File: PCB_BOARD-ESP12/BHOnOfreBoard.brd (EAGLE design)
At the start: 53 x 55 mm, 23 parts, among them J1 4p, J6 8p, J7 8p, K1 OMRON-G3MB-202P-SSR2, K2 OMRON-G3MB-202P-SSR2, Q1 S8050, Q2 S8050, U1 LM1117, U2 esp12

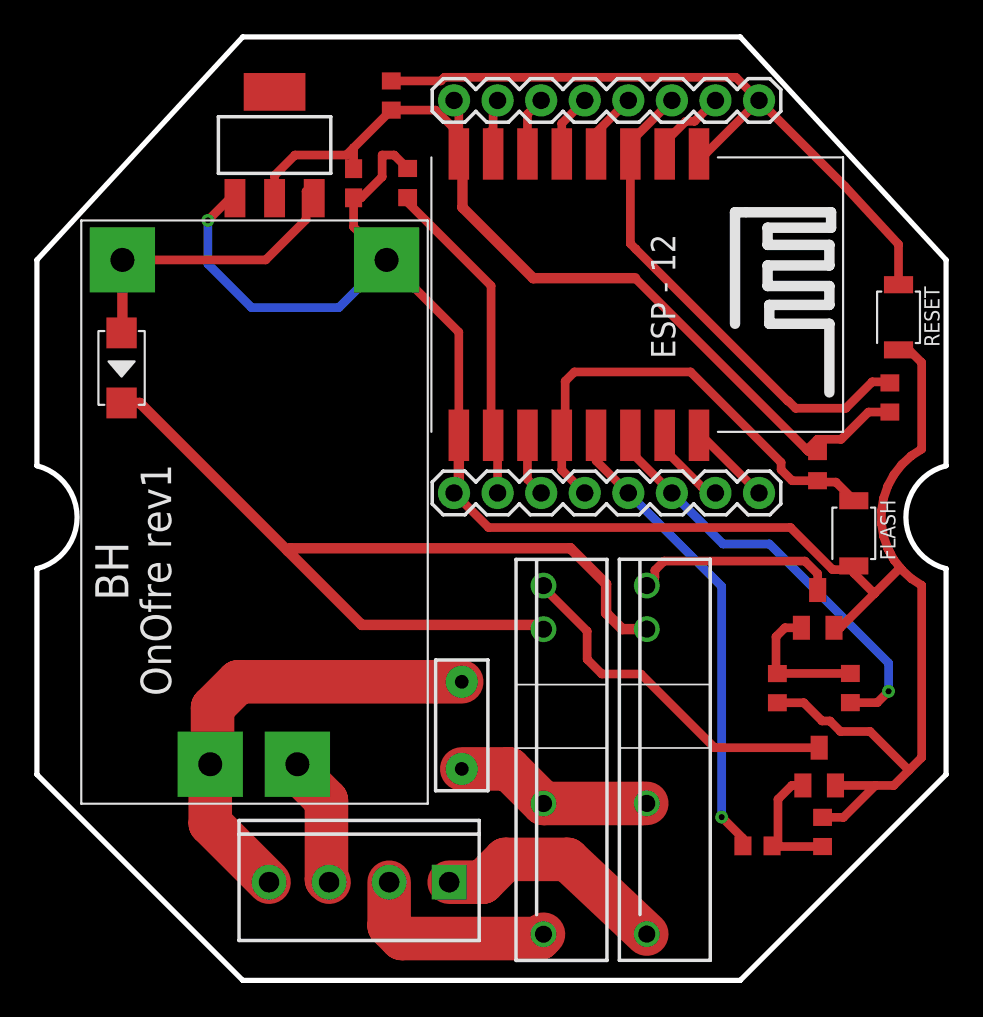
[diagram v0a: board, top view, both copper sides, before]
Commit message: fix relay position
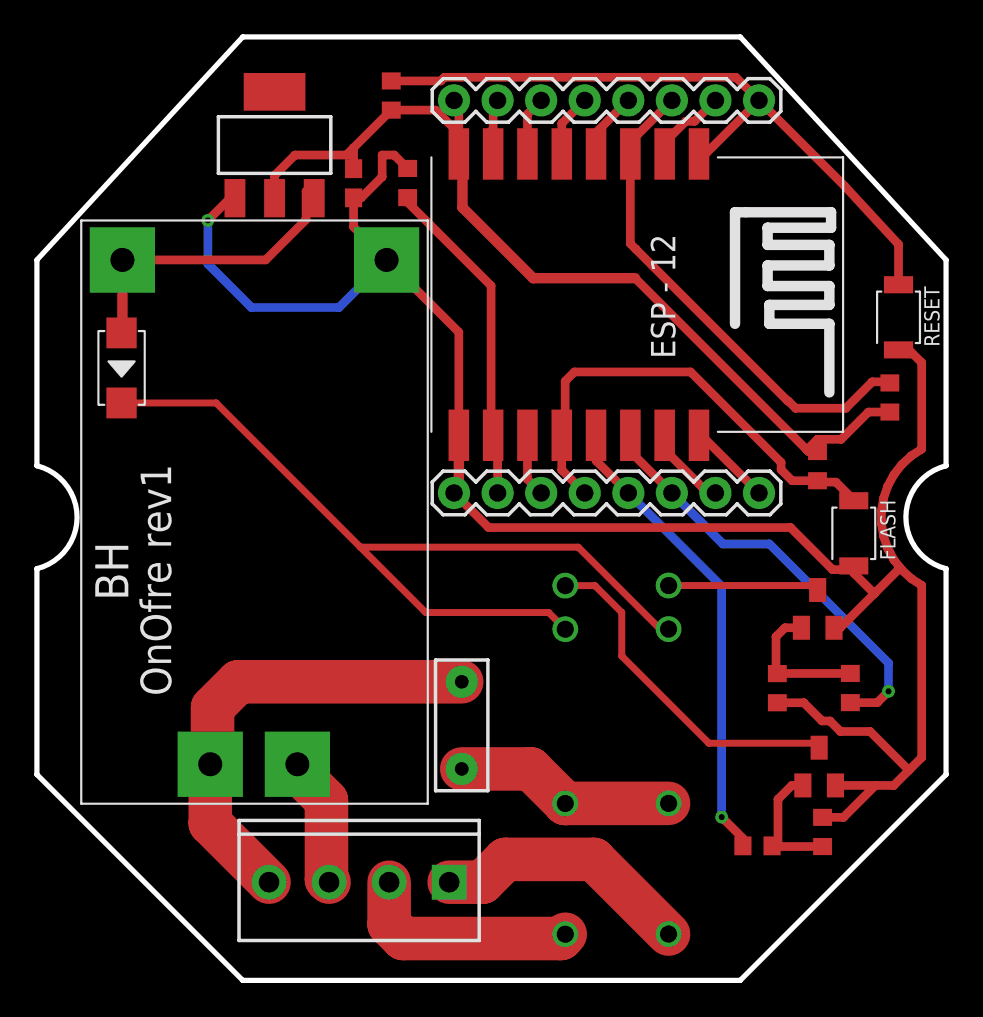
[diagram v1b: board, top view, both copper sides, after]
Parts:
- moved K2 1.27 mm to (37.0, 15.5), flipped to the bottom
- moved K1 1.27 mm to (31.0, 15.5), flipped to the bottom
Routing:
- net N$9: track 12.1 -> 8.80 mm
- net N$2: track 54.0 -> 51.3 mm
- net NEUTRAL_TWO_OUT: track 13.8 -> 15.1 mm
- net NEUTRAL_IN_FUSED: track 11.6 -> 12.9 mm
- net NEUTRAL_ONE_OUT: track 12.0 -> 13.2 mm
- net N$1: track 21.0 -> 20.2 mm
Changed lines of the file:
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@@
 </autorouter>
 <elements>
-<element name="K1" library="Omron G3MB 202p SSR" package="OMRON-G3MB-202P-SSR" value="OMRON-G3MB-202P-SSR2" x="29.7255875" y="15.53723125" smashed="yes" rot="R90">
-<attribute name="MF" value="" x="29.7255875" y="15.53723125" size="1.778" layer="27" rot="R90" display="off"/>
-<attribute name="MPN" value="S202S02F" x="29.7255875" y="15.53723125" size="1.778" layer="27" rot="R90" display="off"/>
-<attribute name="OC_FARNELL" value="1618475" x="29.7255875" y="15.53723125" size="1.778" layer="27" rot="R90" display="off"/>
-<attribute name="OC_NEWARK" value="14N9588" x="29.7255875" y="15.53723125" size="1.778" layer="27" rot="R90" display="off"/>
+<element name="K1" library="Omron G3MB 202p SSR" package="OMRON-G3MB-202P-SSR" value="OMRON-G3MB-202P-SSR2" x="30.9955875" y="15.53723125" smashed="yes" rot="MR90">
+<attribute name="MF" value="" x="30.9955875" y="15.53723125" size="1.778" layer="28" rot="MR90" display="off"/>
+<attribute name="MPN" value="S202S02F" x="30.9955875" y="15.53723125" size="1.778" layer="28" rot="MR90" display="off"/>
+<attribute name="OC_FARNELL" value="1618475" x="30.9955875" y="15.53723125" size="1.778" layer="28" rot="MR90" display="off"/>
+<attribute name="OC_NEWARK" value="14N9588" x="30.9955875" y="15.53723125" size="1.778" layer="28" rot="MR90" display="off"/>
 </element>
 <element name="F1" library="SparkFun-Fuses" library_urn="urn:adsk.eagle:library:517" package="PTH" package3d_urn="urn:adsk.eagle:package:38574/1" value="FUSE 2A" x="24.959440625" y="15.011509375" smashed="yes" rot="R270">
@@
 <attribute name="VALUE" x="20.59235" y="45.182759375" size="1.27" layer="27" rot="R90"/>
 </element>
-<element name="K2" library="Omron G3MB 202p SSR" package="OMRON-G3MB-202P-SSR" value="OMRON-G3MB-202P-SSR2" x="35.747684375" y="15.543271875" smashed="yes" rot="R90">
-<attribute name="MF" value="" x="16.951684375" y="15.543271875" size="1.778" layer="27" rot="R90" display="off"/>
-<attribute name="MPN" value="S202S02F" x="16.951684375" y="15.543271875" size="1.778" layer="27" rot="R90" display="off"/>
-<attribute name="OC_FARNELL" value="1618475" x="16.951684375" y="15.543271875" size="1.778" layer="27" rot="R90" display="off"/>
-<attribute name="OC_NEWARK" value="14N9588" x="16.951684375" y="15.543271875" size="1.778" layer="27" rot="R90" display="off"/>
+<element name="K2" library="Omron G3MB 202p SSR" package="OMRON-G3MB-202P-SSR" value="OMRON-G3MB-202P-SSR2" x="37.017684375" y="15.543271875" smashed="yes" rot="MR90">
+<attribute name="MF" value="" x="55.813684375" y="15.543271875" size="1.778" layer="28" rot="MR90" display="off"/>
+<attribute name="MPN" value="S202S02F" x="55.813684375" y="15.543271875" size="1.778" layer="28" rot="MR90" display="off"/>
+<attribute name="OC_FARNELL" value="1618475" x="55.813684375" y="15.543271875" size="1.778" layer="28" rot="MR90" display="off"/>
+<attribute name="OC_NEWARK" value="14N9588" x="55.813684375" y="15.543271875" size="1.778" layer="28" rot="MR90" display="off"/>
 </element>
 <element name="Q2" library="semicon-smd-ipc" library_urn="urn:adsk.eagle:library:353" package="SOT23" package3d_urn="urn:adsk.eagle:package:26310/1" value="S8050 " x="45.709821875" y="21.800703125" smashed="yes">
@@
 <contactref element="Q1" pad="3"/>
 <contactref element="K1" pad="4"/>
-<wire x1="29.7255875" y1="23.15723125" x2="29.7255875" y2="23.04855625" width="0.508" layer="1"/>
-<wire x1="29.7255875" y1="23.04855625" x2="32.270415625" y2="20.503728125" width="0.508" layer="1"/>
-<wire x1="32.270415625" y1="20.503728125" x2="32.270415625" y2="18.863065625" width="0.508" layer="1"/>
-<wire x1="32.270415625" y1="18.863065625" x2="33.12748125" y2="18.006" width="0.508" layer="1"/>
-<wire x1="35.399703125" y1="18.006" x2="33.12748125" y2="18.006" width="0.508" layer="1"/>
-<wire x1="45.795765625" y1="13.708365625" x2="39.6973375" y2="13.708365625" width="0.508" layer="1"/>
-<wire x1="39.6973375" y1="13.708365625" x2="35.399703125" y2="18.006" width="0.508" layer="1"/>
+<wire x1="39.37" y1="13.97" x2="45.53413125" y2="13.97" width="0.4064" layer="1"/>
+<wire x1="45.53413125" y1="13.97" x2="45.795765625" y2="13.708365625" width="0.4064" layer="1"/>
+<wire x1="30.9955875" y1="23.15723125" x2="32.72276875" y2="23.15723125" width="0.4064" layer="1"/>
+<wire x1="32.72276875" y1="23.15723125" x2="34.29" y2="21.59" width="0.4064" layer="1"/>
+<wire x1="34.29" y1="21.59" x2="34.29" y2="19.05" width="0.4064" layer="1"/>
+<wire x1="34.29" y1="19.05" x2="39.37" y2="13.97" width="0.4064" layer="1"/>
 </signal>
 <signal name="GPIO0">
@@
 <wire x1="24.2265875" y1="5.869178125" x2="26.175546875" y2="5.869178125" width="2.54" layer="1"/>
 <wire x1="26.175546875" y1="5.869178125" x2="27.505796875" y2="7.199428125" width="2.54" layer="1"/>
-<wire x1="27.505796875" y1="7.199428125" x2="31.12295" y2="7.199428125" width="2.54" layer="1"/>
-<wire x1="31.12295" y1="7.199428125" x2="35.747684375" y2="2.843271875" width="2.54" layer="1"/>
+<wire x1="27.505796875" y1="7.199428125" x2="32.661528125" y2="7.199428125" width="2.54" layer="1"/>
+<wire x1="32.661528125" y1="7.199428125" x2="37.017684375" y2="2.843271875" width="2.54" layer="1"/>
 </signal>
 <signal name="NEUTRAL_ONE_OUT">
 <contactref element="K1" pad="1"/>
 <contactref element="J1" pad="2"/>
-<wire x1="20.7265875" y1="5.869178125" x2="20.7265875" y2="3.32599375" width="2.54" layer="1"/>
-<wire x1="20.7265875" y1="3.32599375" x2="21.4689" y2="2.58368125" width="2.54" layer="1"/>
-<wire x1="21.4689" y1="2.58368125" x2="29.4720375" y2="2.58368125" width="2.54" layer="1"/>
-<wire x1="29.4720375" y1="2.58368125" x2="29.7255875" y2="2.83723125" width="2.54" layer="1"/>
+<wire x1="20.7265875" y1="5.869178125" x2="20.7265875" y2="3.4034125" width="2.54" layer="1"/>
+<wire x1="20.7265875" y1="3.4034125" x2="21.54631875" y2="2.58368125" width="2.54" layer="1"/>
+<wire x1="21.54631875" y1="2.58368125" x2="30.7420375" y2="2.58368125" width="2.54" layer="1"/>
+<wire x1="30.7420375" y1="2.58368125" x2="30.9955875" y2="2.83723125" width="2.54" layer="1"/>
 </signal>
 <signal name="N$9">
 <contactref element="Q2" pad="3"/>
 <contactref element="K2" pad="4"/>
-<wire x1="45.709821875" y1="22.900703125" x2="45.709821875" y2="23.84685625" width="0.508" layer="1"/>
-<wire x1="45.709821875" y1="23.84685625" x2="44.967496875" y2="24.58918125" width="0.508" layer="1"/>
-<wire x1="44.967496875" y1="24.58918125" x2="36.756603125" y2="24.58918125" width="0.508" layer="1"/>
-<wire x1="36.756603125" y1="24.58918125" x2="36.219553125" y2="24.05213125" width="0.508" layer="1"/>
-<wire x1="36.219553125" y1="24.05213125" x2="36.219553125" y2="23.635140625" width="0.508" layer="1"/>
-<wire x1="36.219553125" y1="23.635140625" x2="35.747684375" y2="23.163271875" width="0.508" layer="1"/>
+<wire x1="37.017684375" y1="23.163271875" x2="45.447253125" y2="23.163271875" width="0.4064" layer="1"/>
+<wire x1="45.447253125" y1="23.163271875" x2="45.709821875" y2="22.900703125" width="0.4064" layer="1"/>
 </signal>
 <signal name="N$13">
@@
 <contactref element="K2" pad="2"/>
 <contactref element="K1" pad="2"/>
-<wire x1="24.959440625" y1="12.471509375" x2="27.711309375" y2="12.471509375" width="2.54" layer="1"/>
-<wire x1="27.711309375" y1="12.471509375" x2="29.7255875" y2="10.45723125" width="2.54" layer="1"/>
-<wire x1="29.7255875" y1="10.45723125" x2="35.473065625" y2="10.45723125" width="2.54" layer="1"/>
-<wire x1="35.473065625" y1="10.45723125" x2="35.747684375" y2="10.463271875" width="2.54" layer="1"/>
+<wire x1="24.959440625" y1="12.471509375" x2="28.981309375" y2="12.471509375" width="2.54" layer="1"/>
+<wire x1="30.9955875" y1="10.45723125" x2="28.981309375" y2="12.471509375" width="2.54" layer="1"/>
+<wire x1="37.017684375" y1="10.463271875" x2="31.001628125" y2="10.463271875" width="2.54" layer="1"/>
+<wire x1="31.001628125" y1="10.463271875" x2="30.9955875" y2="10.45723125" width="2.54" layer="1"/>
 </signal>
 <signal name="N$2">
@@
 <contactref element="K2" pad="3"/>
 <contactref element="K1" pad="3"/>
-<wire x1="5.12860625" y1="33.807096875" x2="6.193215625" y2="33.807096875" width="0.6096" layer="1"/>
-<wire x1="14.820109375" y1="25.180203125" x2="6.193215625" y2="33.807096875" width="0.6096" layer="1"/>
-<wire x1="14.820109375" y1="25.180203125" x2="19.131984375" y2="20.868328125" width="0.6096" layer="1"/>
-<wire x1="19.131984375" y1="20.868328125" x2="29.474490625" y2="20.868328125" width="0.6096" layer="1"/>
-<wire x1="29.474490625" y1="20.868328125" x2="29.7255875" y2="20.61723125" width="0.6096" layer="1"/>
-<wire x1="35.747684375" y1="20.623271875" x2="34.3132125" y2="20.623271875" width="0.6096" layer="1"/>
-<wire x1="34.3132125" y1="20.623271875" x2="33.3751125" y2="21.561371875" width="0.6096" layer="1"/>
-<wire x1="33.3751125" y1="21.561371875" x2="33.3751125" y2="23.255884375" width="0.6096" layer="1"/>
-<wire x1="33.3751125" y1="23.255884375" x2="31.296384375" y2="25.3346125" width="0.6096" layer="1"/>
-<wire x1="31.296384375" y1="25.3346125" x2="14.97451875" y2="25.3346125" width="0.6096" layer="1"/>
-<wire x1="14.97451875" y1="25.3346125" x2="14.820109375" y2="25.180203125" width="0.6096" layer="1"/>
+<wire x1="5.12860625" y1="33.807096875" x2="10.642903125" y2="33.807096875" width="0.4064" layer="1"/>
+<wire x1="19.05" y1="25.4" x2="10.642903125" y2="33.807096875" width="0.4064" layer="1"/>
+<wire x1="19.05" y1="25.4" x2="22.86" y2="21.59" width="0.4064" layer="1"/>
+<wire x1="22.86" y1="21.59" x2="30.02281875" y2="21.59" width="0.4064" layer="1"/>
+<wire x1="30.02281875" y1="21.59" x2="30.9955875" y2="20.61723125" width="0.4064" layer="1"/>
+<wire x1="37.017684375" y1="20.623271875" x2="36.526728125" y2="20.623271875" width="0.4064" layer="1"/>
+<wire x1="36.526728125" y1="20.623271875" x2="31.75" y2="25.4" width="0.4064" layer="1"/>
+<wire x1="31.75" y1="25.4" x2="19.05" y2="25.4" width="0.4064" layer="1"/>
 </signal>
 <signal name="N$7">
